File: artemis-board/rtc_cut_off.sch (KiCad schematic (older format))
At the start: 7 parts, among them Q1 2N7002, U7 PCF8563T, U9 TCA6408A, Y2 32.768KHz

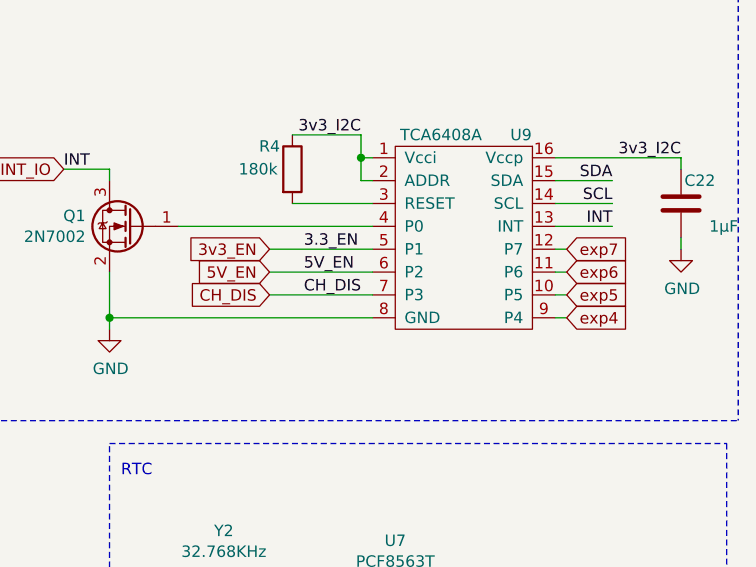
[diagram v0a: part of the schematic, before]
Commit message: renamed net lables, disconnected en lines from header and deleted unused
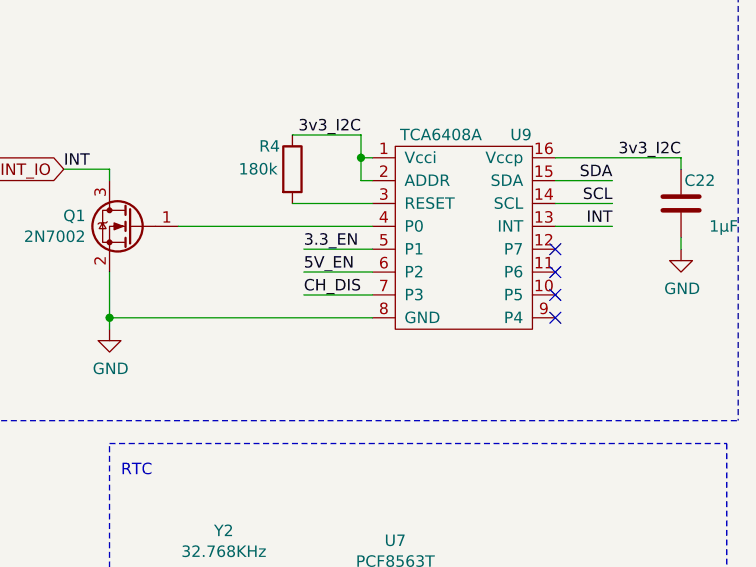
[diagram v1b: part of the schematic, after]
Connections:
- net 3v3_EN renamed 3v3V_EN
- net CH_DIS renamed CHARGE-DISABLE
- net exp4: no longer names the net of U9.9 (P4)
- net exp5: no longer names the net of U9.10 (P5)
- net exp6: no longer names the net of U9.11 (P6)
- net exp7: no longer names the net of U9.12 (P7)
- no-connect marks 2 -> 6
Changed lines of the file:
@@
 $Descr A4 11693 8268
 encoding utf-8
-Sheet 6 6
+Sheet 5 6
 Title "SuperPower-uC"
 Date "2020-09-20"
@@
 Wire Notes Line
 	6700 1850 6700 4000
-Wire Wire Line
-	5950 3250 5900 3250
-Wire Wire Line
-	5900 3350 5950 3350
-Wire Wire Line
-	5950 3450 5900 3450
-Wire Wire Line
-	5900 3550 5950 3550
-Text GLabel 5950 3250 2    50   Input ~ 0
-exp7
-Text GLabel 5950 3350 2    50   Input ~ 0
-exp6
-Text GLabel 5950 3450 2    50   Input ~ 0
-exp5
-Text GLabel 5950 3550 2    50   Input ~ 0
-exp4
-Wire Wire Line
-	4650 3450 5100 3450
-Wire Wire Line
-	4650 3350 5100 3350
-Wire Wire Line
-	4650 3250 5100 3250
-Text GLabel 4650 3250 0    50   Input ~ 0
-3v3_EN
-Text GLabel 4650 3350 0    50   Input ~ 0
-5V_EN
-Text GLabel 4650 3450 0    50   Input ~ 0
-CH_DIS
 Text Label 4800 3250 0    50   ~ 0
 3.3_EN
@@
 Text Label 6450 4750 2    50   ~ 0
 3v3_I2C
+Wire Wire Line
+	4800 3250 5100 3250
+Wire Wire Line
+	5100 3350 4800 3350
+Wire Wire Line
+	4800 3450 5100 3450
+NoConn ~ 5900 3550
+NoConn ~ 5900 3450
+NoConn ~ 5900 3350
+NoConn ~ 5900 3250
 $EndSCHEMATC

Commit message: fixed erc
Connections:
- net INT_IO renamed INT
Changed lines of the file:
@@
 Wire Notes Line
 	550  600  550  2450
-Text GLabel 3750 2900 0    50   Input ~ 0
-INT_IO
 Text Notes 3400 2150 0    50   ~ 0
 If not populated add pulldowns to the 3v3 and 5v EN pins
-Text HLabel 1350 1300 0    50   Input ~ 0
-VBAT
-Wire Wire Line
-	1350 1300 1750 1300
-Text Label 1750 1300 2    50   ~ 0
-VBAT
 Text Label 6450 4750 2    50   ~ 0
 3v3_I2C

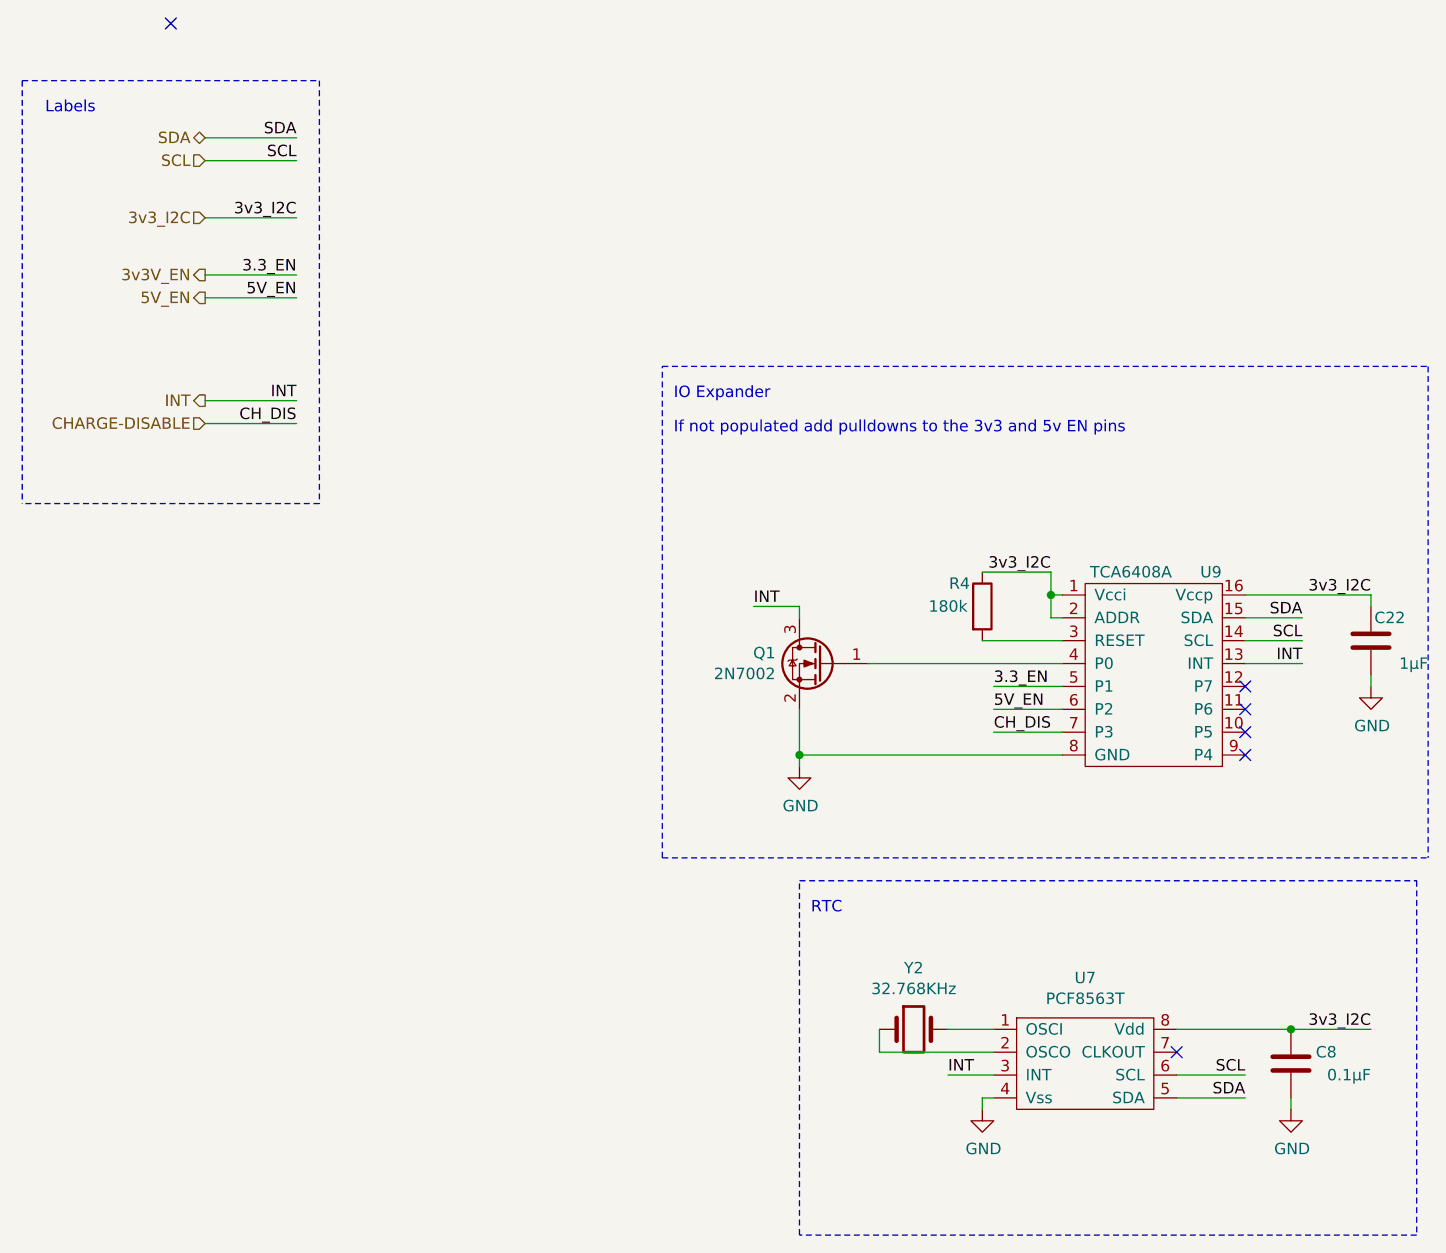
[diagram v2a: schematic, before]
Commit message: connected io expanders Vccp pin to Vbat instead of Vcc_I2c
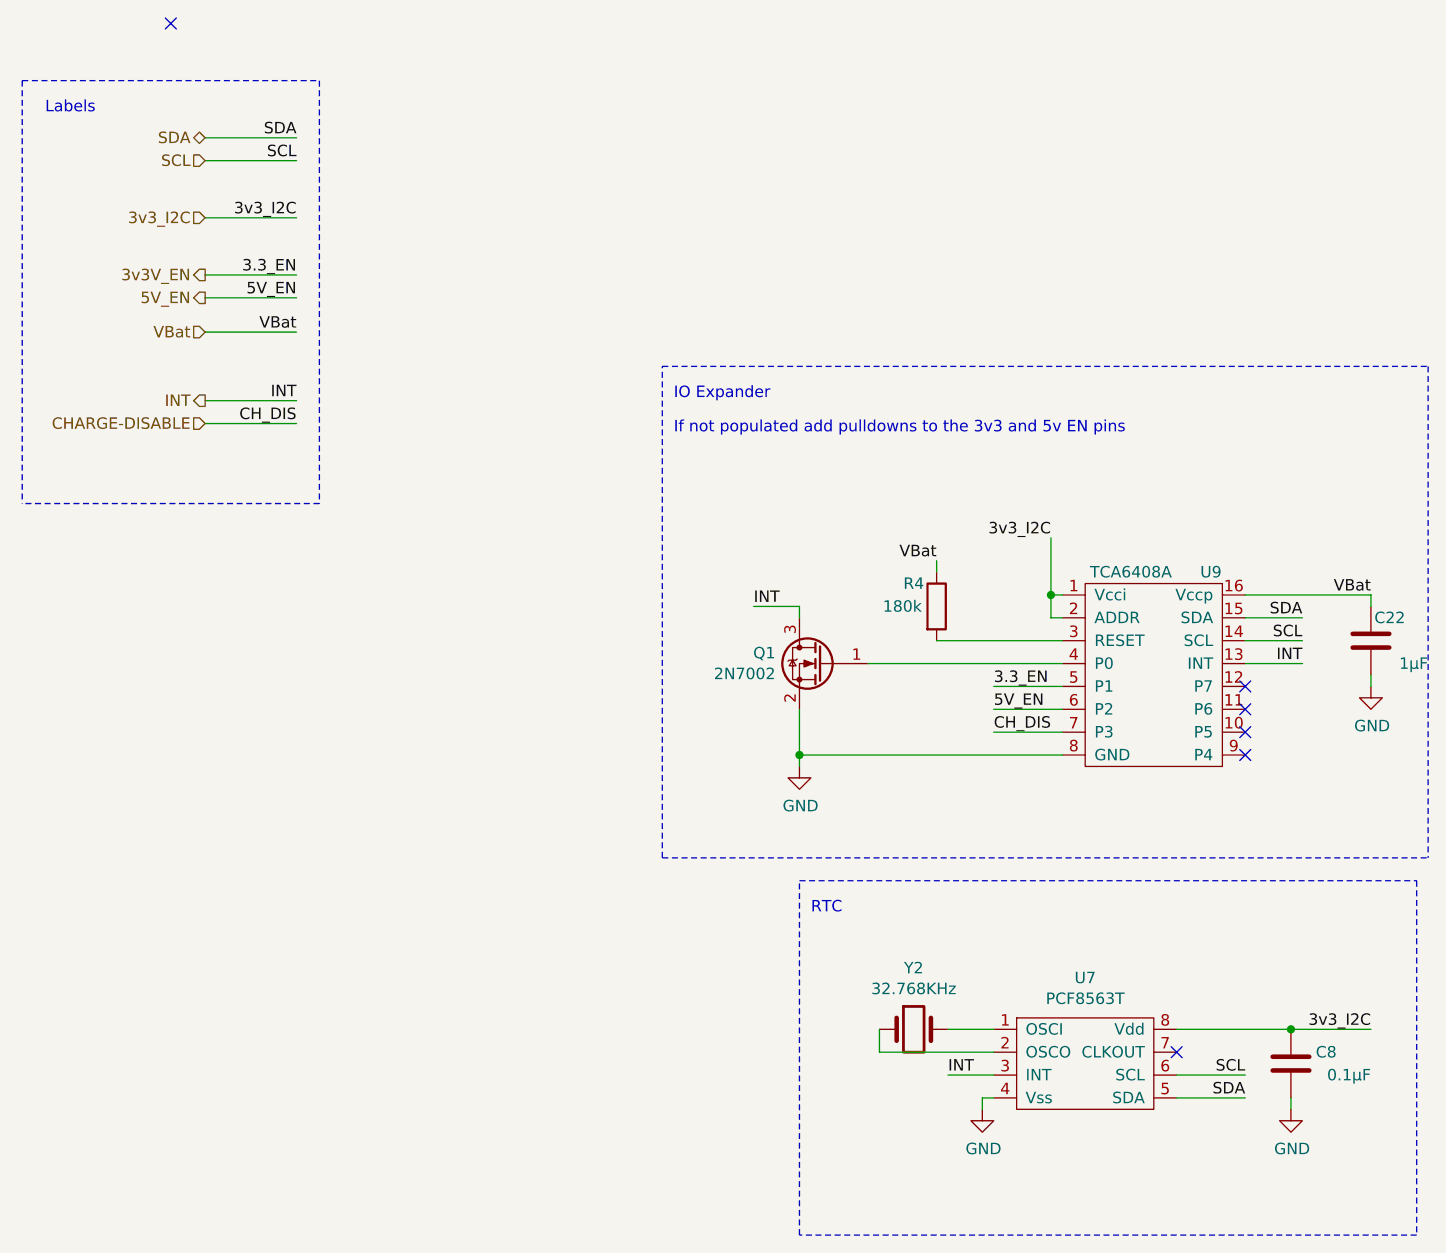
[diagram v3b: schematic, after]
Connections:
- net 3v3_I2C: no longer C22.2, R4.1, U9.16 (Vccp)
- new net VBat: C22.2, R4.1, U9.16 (Vccp)
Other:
- moved on the sheet: R4
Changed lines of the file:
@@
 L Device:R R4
 U 1 1 5FC6F3D4
-P 4750 2900
-F 0 "R4" H 4650 3000 50  0000 C CNN
-F 1 "180k" H 4600 2900 50  0000 C CNN
-F 2 "Resistor_SMD:R_0603_1608Metric_Pad1.05x0.95mm_HandSolder" V 4680 2900 50  0001 C CNN
-F 3 "~" H 4750 2900 50  0001 C CNN
-F 4 "C22827" H 4750 2900 50  0001 C CNN "LCSC"
-	1    4750 2900
+P 4550 2900
+F 0 "R4" H 4450 3000 50  0000 C CNN
+F 1 "180k" H 4400 2900 50  0000 C CNN
+F 2 "Resistor_SMD:R_0603_1608Metric_Pad1.05x0.95mm_HandSolder" V 4480 2900 50  0001 C CNN
+F 3 "~" H 4550 2900 50  0001 C CNN
+F 4 "C22827" H 4550 2900 50  0001 C CNN "LCSC"
+	1    4550 2900
 	1    0    0    -1
 $EndComp
 Wire Wire Line
-	4750 3050 5100 3050
-Wire Wire Line
-	4750 2750 5050 2750
-Wire Wire Line
-	5050 2750 5050 2850
-Text Label 5050 2750 2    50   ~ 0
+	5050 2600 5050 2850
+Text Label 5050 2600 2    50   ~ 0
 3v3_I2C
 Wire Wire Line
 	4250 3150 5100 3150
-Wire Wire Line
-	5100 2950 5050 2950
-Wire Wire Line
-	5050 2950 5050 2850
-Connection ~ 5050 2850
-Text Label 6450 2850 2    50   ~ 0
-3v3_I2C
 $Comp
 L Device:C C22
@@
 NoConn ~ 5900 3350
 NoConn ~ 5900 3250
+Wire Wire Line
+	4550 3050 5100 3050
+Text HLabel 1350 1700 0    50   Input ~ 0
+VBat
+Text Label 1750 1700 2    50   ~ 0
+VBat
+Wire Wire Line
+	1750 1700 1350 1700
+Text Label 4550 2700 2    50   ~ 0
+VBat
+Wire Wire Line
+	4550 2750 4550 2700
+Text Label 6450 2850 2    50   ~ 0
+VBat
+Wire Wire Line
+	5100 2950 5050 2950
+Wire Wire Line
+	5050 2950 5050 2850
+Connection ~ 5050 2850
 $EndSCHEMATC

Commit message: added pulldown to Q1 and inverter to CH_DIS
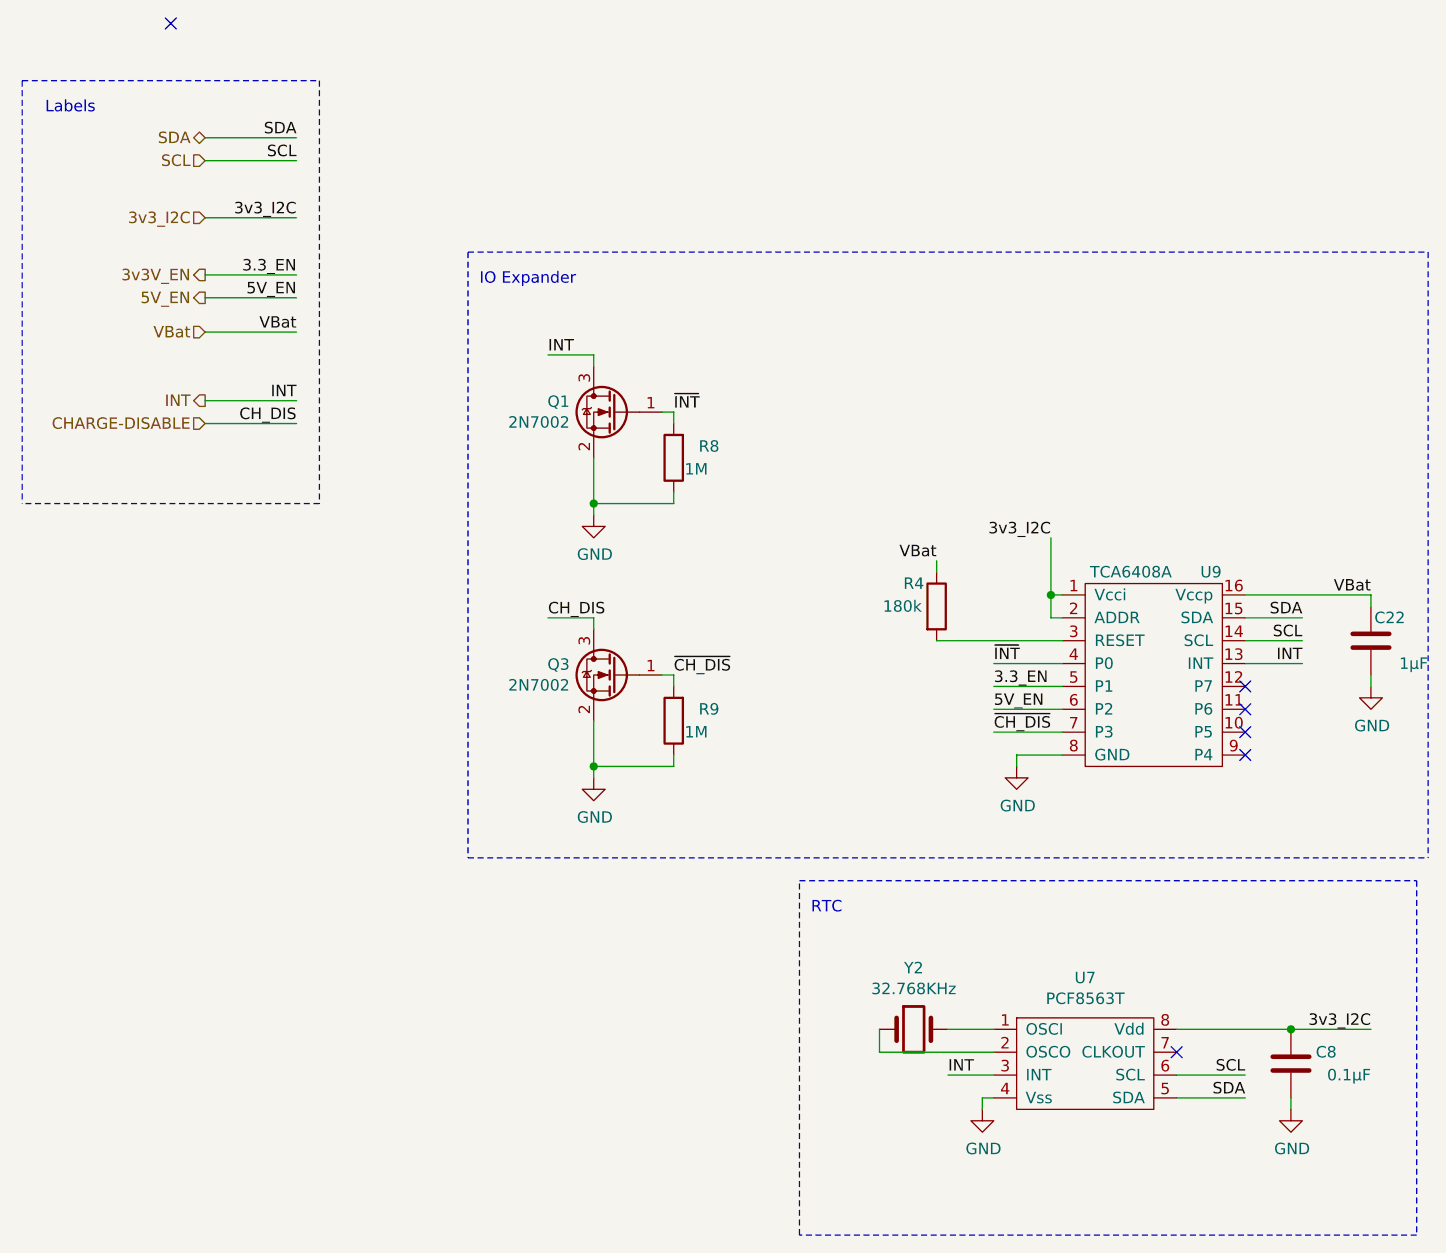
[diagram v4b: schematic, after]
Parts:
- added Q3: 2N7002, Package_TO_SOT_SMD:SOT-23, symbol Transistor_FET:2N7002
- added R8, R9: 1M, Resistor_SMD:R_0603_1608Metric_Pad1.05x0.95mm_HandSolder, symbol Device:R
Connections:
- net CHARGE-DISABLE: now also Q3.3 (D); no longer U9.7 (P3)
- net GND: now also Q3.2 (S), R8.1, R9.1
- net ~INT: now reaches Q1.1 (G), U9.4 (P0)
- net ~INT: now also R8.2
- new net ~CH_DIS: Q3.1 (G), R9.2, U9.7 (P3)
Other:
- note removed: "If not populated add pulldowns to the 3v3 and 5v EN pins"
- moved on the sheet: Q1
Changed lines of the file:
@@
 L power:GND #PWR0109
 U 1 1 5F81AC3F
-P 3950 3600
-F 0 "#PWR0109" H 3950 3350 50  0001 C CNN
-F 1 "GND" H 3955 3427 50  0000 C CNN
-F 2 "" H 3950 3600 50  0001 C CNN
-F 3 "" H 3950 3600 50  0001 C CNN
-	1    3950 3600
-	1    0    0    -1
-$EndComp
-Wire Wire Line
-	3950 3550 3950 3600
+P 3050 2500
+F 0 "#PWR0109" H 3050 2250 50  0001 C CNN
+F 1 "GND" H 3055 2327 50  0000 C CNN
+F 2 "" H 3050 2500 50  0001 C CNN
+F 3 "" H 3050 2500 50  0001 C CNN
+	1    3050 2500
+	1    0    0    -1
+$EndComp
+Wire Wire Line
+	3050 2450 3050 2500
 $Comp
 L Transistor_FET:2N7002 Q1
 U 1 1 5F81E351
-P 4050 3150
-F 0 "Q1" H 4255 3196 50  0000 L CNN
-F 1 "2N7002" H 4255 3105 50  0000 L CNN
-F 2 "Package_TO_SOT_SMD:SOT-23" H 4250 3075 50  0001 L CIN
-F 3 "https://www.fairchildsemi.com/datasheets/2N/2N7002.pdf" H 4050 3150 50  0001 L CNN
-F 4 "" H 4050 3150 50  0001 C CNN "Field4"
-F 5 "C8545" H 4050 3150 50  0001 C CNN "LCSC"
-	1    4050 3150
+P 3150 2050
+F 0 "Q1" H 3355 2096 50  0000 L CNN
+F 1 "2N7002" H 3355 2005 50  0000 L CNN
+F 2 "Package_TO_SOT_SMD:SOT-23" H 3350 1975 50  0001 L CIN
+F 3 "https://www.fairchildsemi.com/datasheets/2N/2N7002.pdf" H 3150 2050 50  0001 L CNN
+F 4 "" H 3150 2050 50  0001 C CNN "Field4"
+F 5 "C8545" H 3150 2050 50  0001 C CNN "LCSC"
+	1    3150 2050
 	-1   0    0    -1
 $EndComp
 Wire Wire Line
-	3950 3350 3950 3550
-Connection ~ 3950 3550
-Wire Wire Line
-	3950 3550 5100 3550
-Wire Wire Line
-	3950 2900 3950 2950
+	3050 2250 3050 2450
+Connection ~ 3050 2450
+Wire Wire Line
+	3050 2450 3400 2450
+Wire Wire Line
+	3050 1800 3050 1850
 Text HLabel 1350 950  0    50   Input ~ 0
 SCL
@@
 Wire Wire Line
 	4600 4950 4800 4950
-Text Label 3750 2900 0    50   ~ 0
-INT
-Wire Wire Line
-	3750 2900 3950 2900
+Text Label 2850 1800 0    50   ~ 0
+INT
+Wire Wire Line
+	2850 1800 3050 1800
 Text Label 6150 3150 2    50   ~ 0
 INT
@@
 Text Notes 4000 4250 0    50   ~ 0
 RTC\n
-Text Notes 3400 2000 0    50   ~ 0
+Text Notes 2550 1500 0    50   ~ 0
 IO Expander
 Text HLabel 1350 2100 0    50   Input ~ 0
@@
 Wire Notes Line
 	1850 2450 550  2450
-Wire Notes Line
-	3350 4000 3350 1850
-Wire Notes Line
-	3350 1850 6700 1850
-Wire Notes Line
-	3350 4000 6700 4000
-Wire Notes Line
-	6700 1850 6700 4000
 Text Label 4800 3250 0    50   ~ 0
 3.3_EN
@@
 5V_EN
 Text Label 4800 3450 0    50   ~ 0
-CH_DIS
+~CH_DIS
 $Comp
 L Device:R R4
@@
 3v3_I2C
 Wire Wire Line
-	4250 3150 5100 3150
+	3350 2050 3400 2050
 $Comp
 L Device:C C22
@@
 Wire Notes Line
 	550  600  550  2450
-Text Notes 3400 2150 0    50   ~ 0
-If not populated add pulldowns to the 3v3 and 5v EN pins
 Text Label 6450 4750 2    50   ~ 0
 3v3_I2C
@@
 	5050 2950 5050 2850
 Connection ~ 5050 2850
+$Comp
+L Device:R R?
+U 1 1 60A05ACF
+P 3400 2250
+AR Path="/5F639F48/60A05ACF" Ref="R?"  Part="1"
+AR Path="/5F63A0E9/60A05ACF" Ref="R?"  Part="1"
+AR Path="/5F63A00B/60A05ACF" Ref="R8"  Part="1"
+F 0 "R8" H 3200 2200 50  0000 L CNN
+F 1 "1M" H 3250 2300 50  0000 L CNN
+F 2 "Resistor_SMD:R_0603_1608Metric_Pad1.05x0.95mm_HandSolder" V 3330 2250 50  0001 C CNN
+F 3 "~" H 3400 2250 50  0001 C CNN
+F 4 "C22935" H 3400 2250 50  0001 C CNN "LCSC"
+	1    3400 2250
+	-1   0    0    1
+$EndComp
+Wire Wire Line
+	3400 2100 3400 2050
+Wire Wire Line
+	3400 2400 3400 2450
+Text Label 4800 3150 0    50   ~ 0
+~INT
+Wire Wire Line
+	4800 3150 5100 3150
+Wire Wire Line
+	5100 3550 4900 3550
+Wire Wire Line
+	4900 3550 4900 3600
+$Comp
+L power:GND #PWR?
+U 1 1 60A0ABA2
+P 4900 3600
+F 0 "#PWR?" H 4900 3350 50  0001 C CNN
+F 1 "GND" H 4905 3427 50  0000 C CNN
+F 2 "" H 4900 3600 50  0001 C CNN
+F 3 "" H 4900 3600 50  0001 C CNN
+	1    4900 3600
+	1    0    0    -1
+$EndComp
+Wire Notes Line
+	6700 1350 6700 4000
+Wire Notes Line
+	2500 1350 2500 4000
+Wire Notes Line
+	2500 1350 6700 1350
+Wire Notes Line
+	2500 4000 6700 4000
+Text Label 3400 2050 0    50   ~ 0
+~INT
+$Comp
+L power:GND #PWR?
+U 1 1 60A20A9C
+P 3050 3650
+F 0 "#PWR?" H 3050 3400 50  0001 C CNN
+F 1 "GND" H 3055 3477 50  0000 C CNN
+F 2 "" H 3050 3650 50  0001 C CNN
+F 3 "" H 3050 3650 50  0001 C CNN
+	1    3050 3650
+	1    0    0    -1
+$EndComp
+Wire Wire Line
+	3050 3600 3050 3650
+$Comp
+L Transistor_FET:2N7002 Q3
+U 1 1 60A20AA5
+P 3150 3200
+F 0 "Q3" H 3355 3246 50  0000 L CNN
+F 1 "2N7002" H 3355 3155 50  0000 L CNN
+F 2 "Package_TO_SOT_SMD:SOT-23" H 3350 3125 50  0001 L CIN
+F 3 "https://www.fairchildsemi.com/datasheets/2N/2N7002.pdf" H 3150 3200 50  0001 L CNN
+F 4 "" H 3150 3200 50  0001 C CNN "Field4"
+F 5 "C8545" H 3150 3200 50  0001 C CNN "LCSC"
+	1    3150 3200
+	-1   0    0    -1
+$EndComp
+Wire Wire Line
+	3050 3400 3050 3600
+Connection ~ 3050 3600
+Wire Wire Line
+	3050 3600 3400 3600
+Wire Wire Line
+	3050 2950 3050 3000
+Text Label 2850 2950 0    50   ~ 0
+CH_DIS
+Wire Wire Line
+	2850 2950 3050 2950
+Wire Wire Line
+	3350 3200 3400 3200
+$Comp
+L Device:R R?
+U 1 1 60A20AB3
+P 3400 3400
+AR Path="/5F639F48/60A20AB3" Ref="R?"  Part="1"
+AR Path="/5F63A0E9/60A20AB3" Ref="R?"  Part="1"
+AR Path="/5F63A00B/60A20AB3" Ref="R9"  Part="1"
+F 0 "R9" H 3200 3350 50  0000 L CNN
+F 1 "1M" H 3250 3450 50  0000 L CNN
+F 2 "Resistor_SMD:R_0603_1608Metric_Pad1.05x0.95mm_HandSolder" V 3330 3400 50  0001 C CNN
+F 3 "~" H 3400 3400 50  0001 C CNN
+F 4 "C22935" H 3400 3400 50  0001 C CNN "LCSC"
+	1    3400 3400
+	-1   0    0    1
+$EndComp
+Wire Wire Line
+	3400 3250 3400 3200
+Wire Wire Line
+	3400 3550 3400 3600
+Text Label 3400 3200 0    50   ~ 0
+~CH_DIS
 $EndSCHEMATC
